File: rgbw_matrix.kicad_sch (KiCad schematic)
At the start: 47 parts, among them IC1 TLC59283DBQR, IC2 TLC59283DBQR, IC3 TLC59283DBQR, IC4 TLC59283DBQR, IC5 TLC59283DBQR, IC6 TLC59283DBQR, J1 Conn_01x07_Female

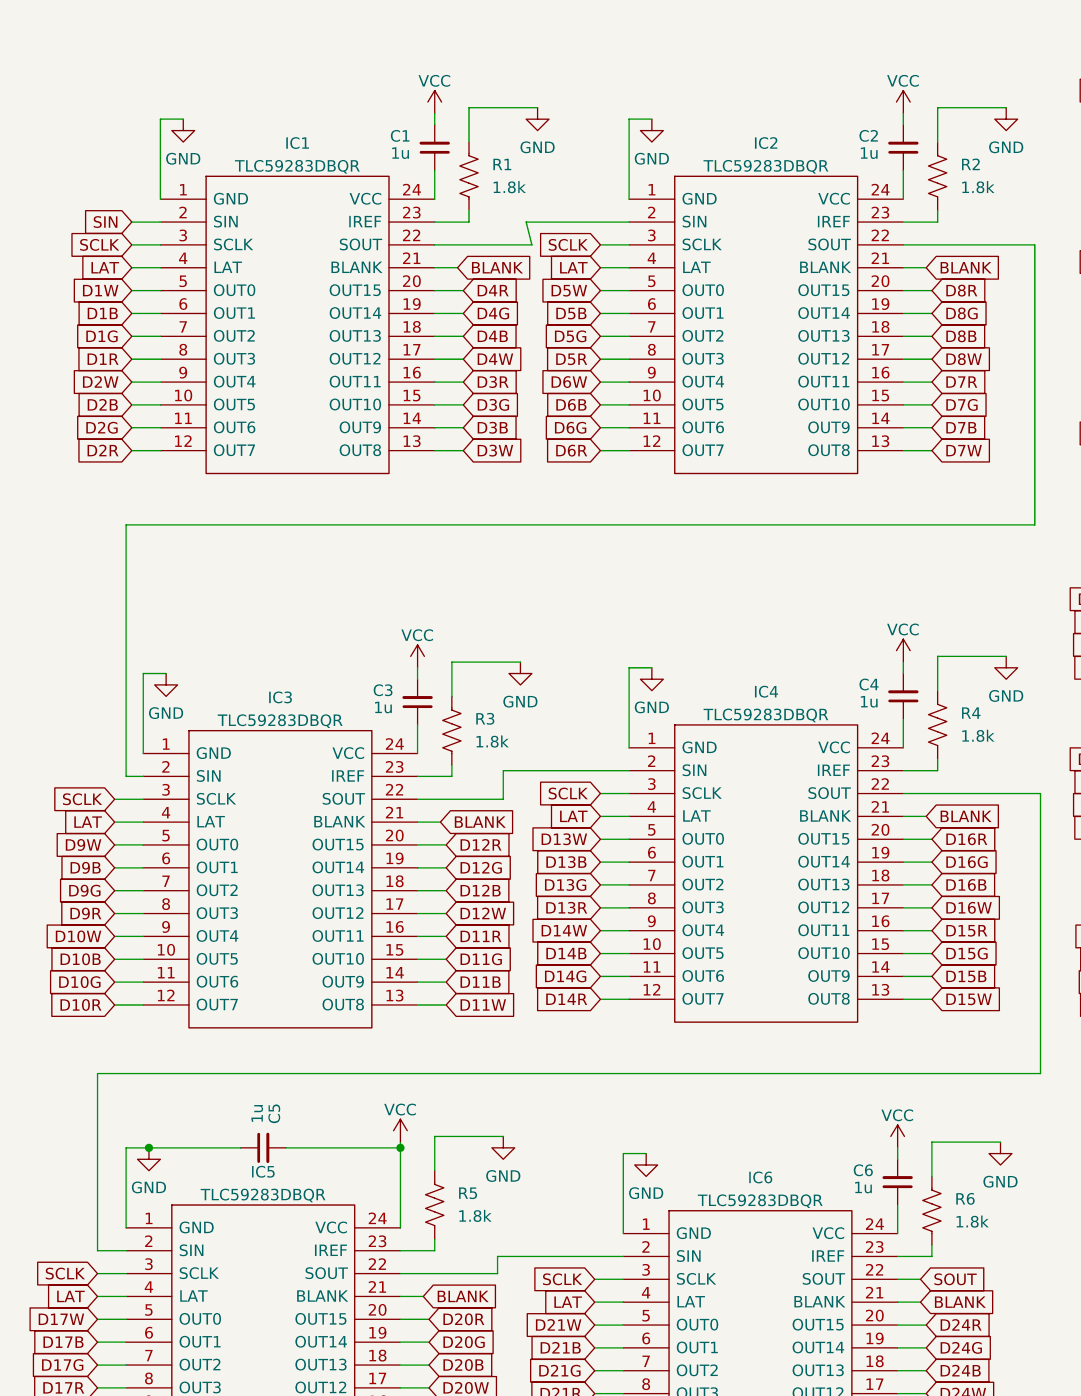
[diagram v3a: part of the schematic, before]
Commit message: capacitors fixed
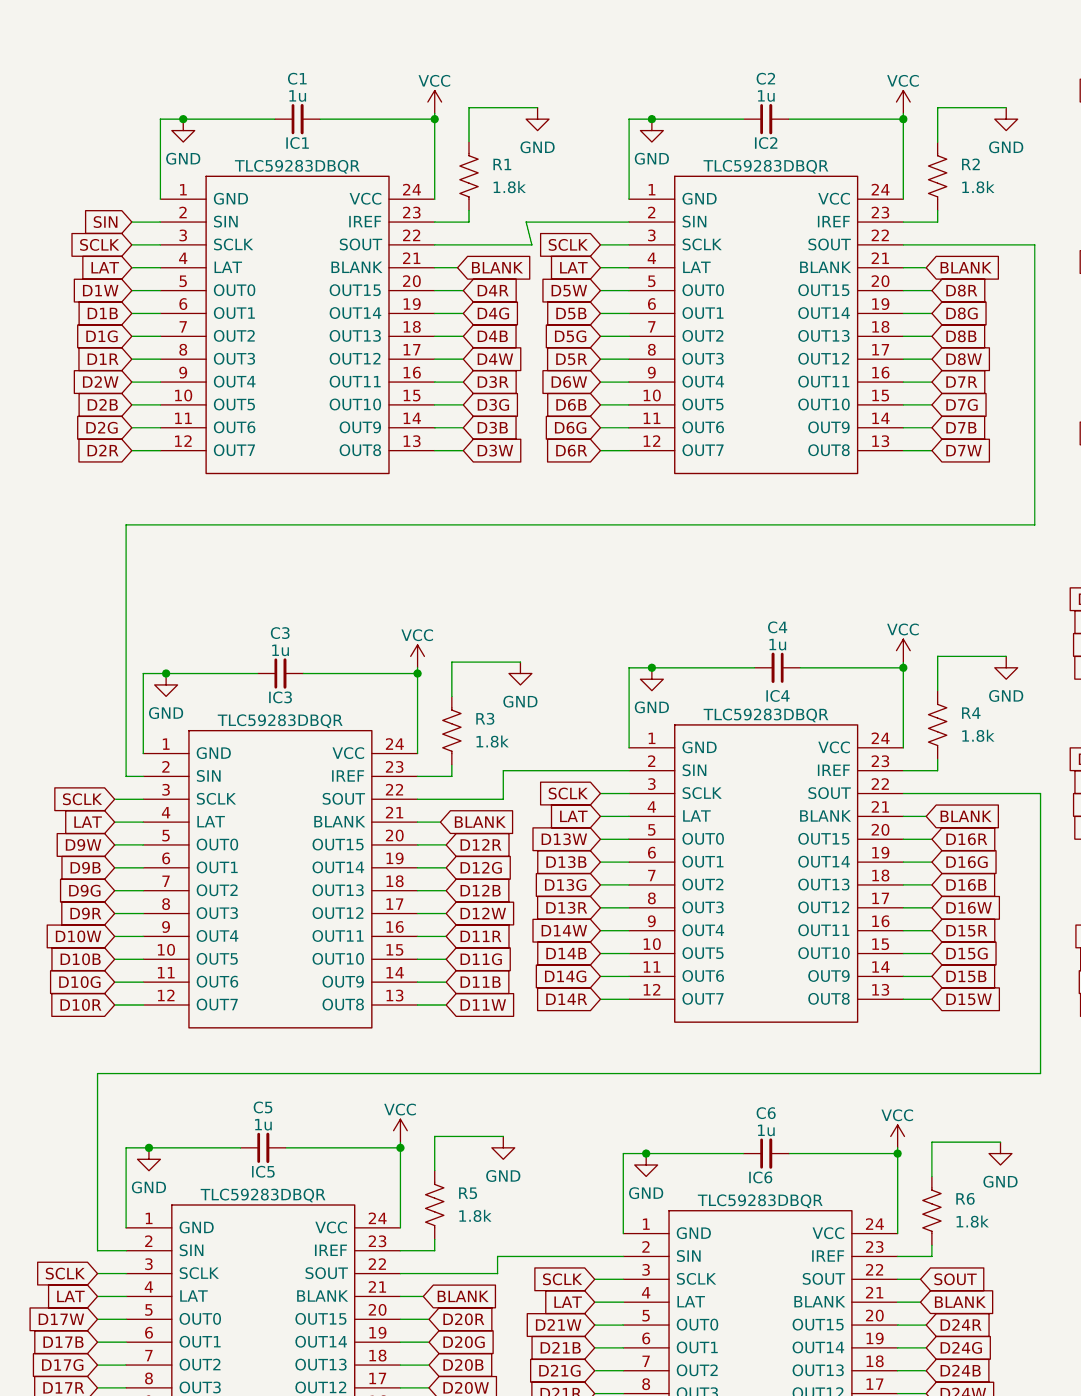
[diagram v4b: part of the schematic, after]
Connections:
- net GND: now also C1.1, C2.1, C3.1, C4.2, C6.1
- net VCC: now also C4.1, IC1.24 (VCC), IC2.24 (VCC), IC3.24 (VCC), IC4.24 (VCC), IC6.24 (VCC); no longer C4.2
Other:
- moved on the sheet: C1, C2, C3, C4, C6
